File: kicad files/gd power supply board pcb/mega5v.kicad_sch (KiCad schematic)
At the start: 14 parts, among them U3 TPS563240DDCR

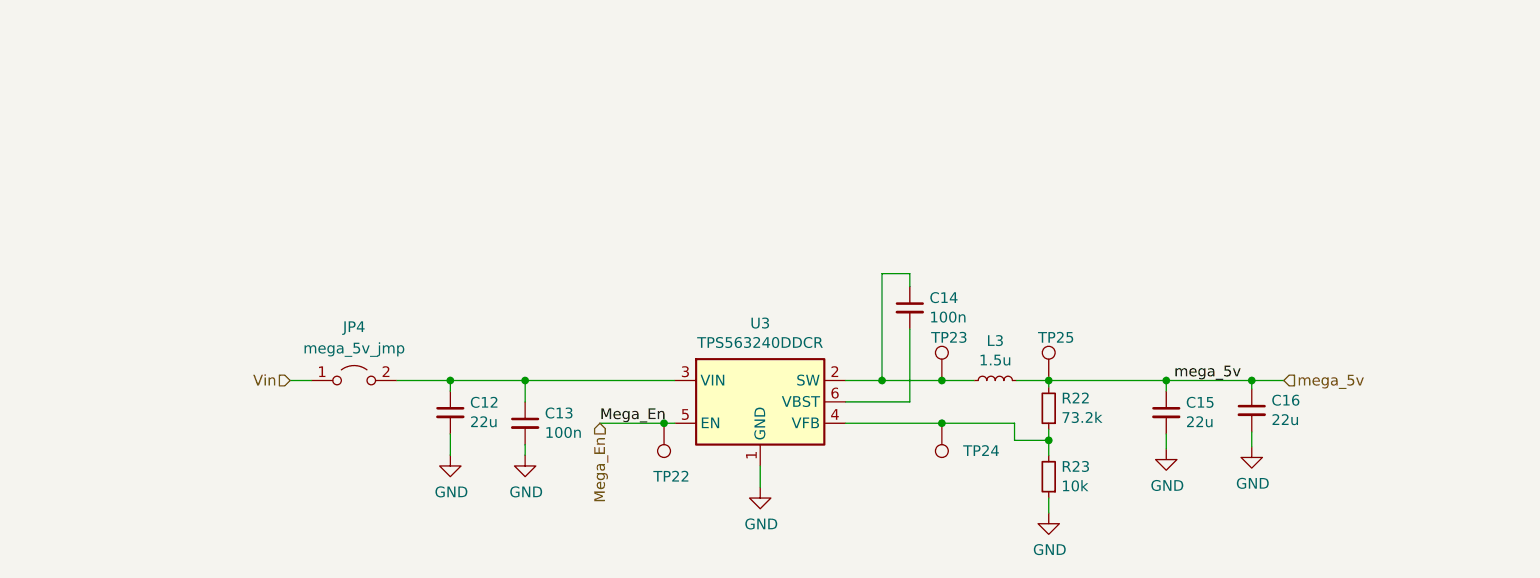
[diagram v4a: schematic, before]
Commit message: added filters and ripped up the board
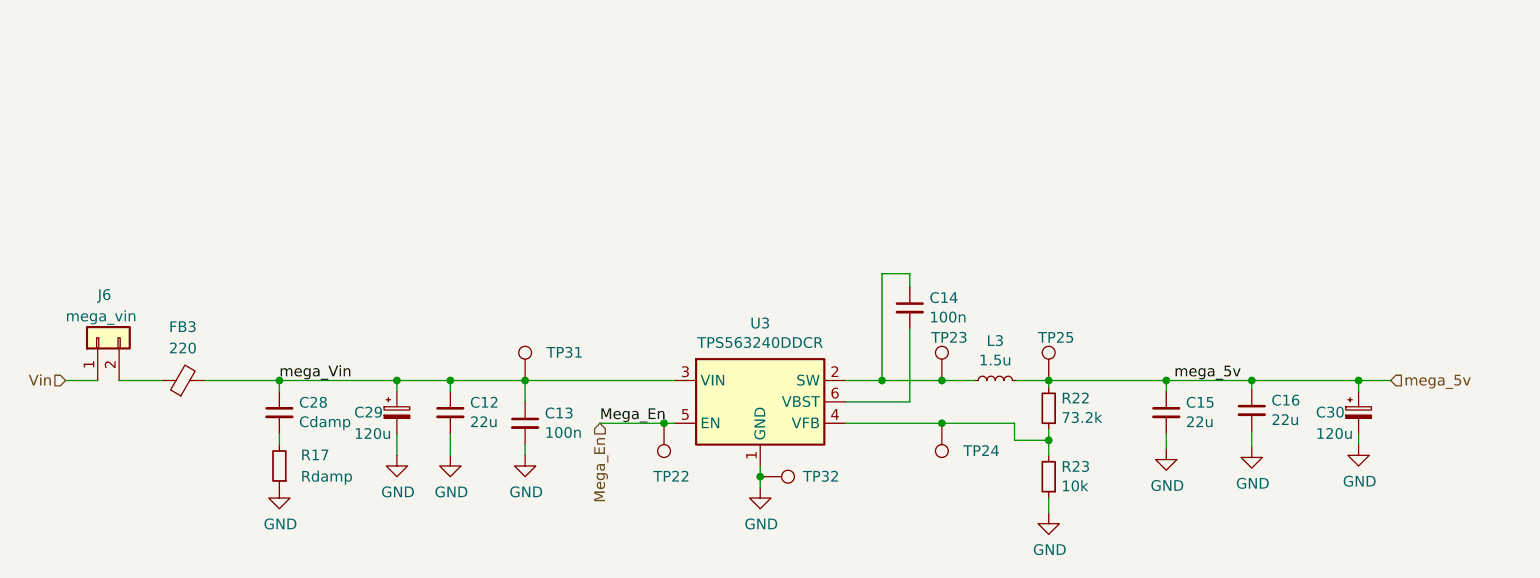
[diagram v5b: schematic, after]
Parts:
- removed JP4: mega_5v_jmp, Jumper:SolderJumper-2_P1.3mm_Open_TrianglePad1.0x1.5mm, symbol Jumper:Jumper_2_Open
- added C28: Cdamp, Capacitor_SMD:C_0805_2012Metric_Pad1.18x1.45mm_HandSolder, symbol Device:C_Small
- added C29, C30: 120u, Capacitor_THT:CP_Radial_D8.0mm_P3.80mm, symbol Device:C_Polarized_Small
- added FB3: 220, Inductor_SMD:L_0603_1608Metric_Pad1.05x0.95mm_HandSolder, symbol Device:FerriteBead_Small
- added J6: mega_vin, Connector_PinHeader_2.54mm:PinHeader_1x02_P2.54mm_Vertical, symbol Connector_Generic:Conn_01x02
- added R17: Rdamp, Resistor_SMD:R_0805_2012Metric_Pad1.20x1.40mm_HandSolder, symbol My Library:R_0805
- added TP31: TestPoint_Harwin, My Libraries:Harwin-S1751-46-Test-Point, symbol My Library:TestPoint_Harwin
- added TP32: TestPoint_Harwin, TestPoint:TestPoint_Pad_1.0x1.0mm, symbol My Library:TestPoint_Harwin
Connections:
- net GND: now also C29.2, C30.2, R17.1, TP32.1
- net Vin: now also J6.1 (Pin_1)
- net mega_5v: now also C30.1
- net mega_Vin: now reaches C12.1, C13.1, U3.3 (VIN)
- net mega_Vin: now also C28.1, C29.1, FB3.2, TP31.1
- new net: FB3.1, J6.2 (Pin_2)
- new net: C28.2, R17.2

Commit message: Updated title blocks for rev2
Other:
- company: (none) -> twitch.tv/baldengineer
- title: (none) -> GD Power Supply Prototype
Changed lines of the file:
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@@
 (kicad_sch (version 20211123) (generator eeschema)
   (paper "A4")
+  (title_block
+    (title "GD Power Supply Prototype")
+    (date "2022-05-16")
+    (rev "Rev 2")
+    (company "twitch.tv/baldengineer")
+  )
   (junction (at 80.01 93.98) (diameter 0) (color 0 0 0 0)
   )
